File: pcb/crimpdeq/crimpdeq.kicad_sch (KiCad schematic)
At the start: 53 parts, among them J2 USB4105-GF-A, Q1 S8550, Q2 DMG3415U, SW1 SW_Push, SW2 SW_Push, U1 ESP32-C3-MINI-1, U2 MCP73831T-2ACI/OT, U3 HX711, U4 Rust_Board, U6 SY8088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

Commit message: fix: add assembly notes for manufacturing
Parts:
- J2: AssemblyNote (none) -> Approved alternate: TYPE-C-31-M-12 may be assembled if foot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
- Q1: AssemblyNote (none) -> TH part: assemble TO-92 inline S8550 only. Do not substitut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
- R12: AssemblyNote (none) -> Critical value: 33kΩ 0402 resistor. Do not use 10kΩ.
- R5: AssemblyNote (none) -> Critical value: 12kΩ 0402 resistor. Do not use 100kΩ.
- R6: AssemblyNote (none) -> Critical value: 8.2kΩ 0402 resistor. Do not use 100kΩ.
- R7, R8: AssemblyNote (none) -> Critical value: 100Ω 0402 resistor. Do not use 100kΩ.
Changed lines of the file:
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@@
 			)
 		)
+		(property "AssemblyNote" "Critical value: 33kΩ 0402 resistor. Do not use 10kΩ."
+			(at 172.72 71.12 0)
+			(effects
+				(font
+					(size 1.27 1.27)
+				)
+				(hide yes)
+			)
+		)
 		(pin "1"
 		)
@@
 			)
 		)
+		(property "AssemblyNote" "Critical value: 12kΩ 0402 resistor. Do not use 100kΩ."
+			(at 72.39 137.16 0)
+			(effects
+				(font
+					(size 1.27 1.27)
+				)
+				(hide yes)
+			)
+		)
 		(pin "1"
 		)
@@
 			)
 		)
+		(property "AssemblyNote" "TH part: assemble TO-92 inline S8550 only. Do not substitute an SMD package."
+			(at 74.93 125.73 0)
+			(effects
+				(font
+					(size 1.27 1.27)
+				)
+				(hide yes)
+			)
+		)
 		(pin "1"
 		)
@@
 			)
 		)
+		(property "AssemblyNote" "Approved alternate: TYPE-C-31-M-12 may be assembled if footprint, pinout, and shell tabs match USB4105-GF-A."
+			(at 213.36 39.37 0)
+			(effects
+				(font
+					(size 1.27 1.27)
+				)
+				(hide yes)
+			)
+		)
 		(pin "A1_B12"
 		)
@@
 			)
 		)
+		(property "AssemblyNote" "Critical value: 8.2kΩ 0402 resistor. Do not use 100kΩ."
+			(at 67.31 140.97 0)
+			(effects
+				(font
+					(size 1.27 1.27)
+				)
+				(hide yes)
+			)
+		)
 		(pin "1"
 		)
@@
 			)
 		)
+		(property "AssemblyNote" "Critical value: 100Ω 0402 resistor. Do not use 100kΩ."
+			(at 31.75 146.05 0)
+			(effects
+				(font
+					(size 1.27 1.27)
+				)
+				(hide yes)
+			)
+		)
 		(pin "1"
 		)
@@
 			(at 31.75 153.67 0)
 			(effects
+				(font
+					(size 1.27 1.27)
+				)
+				(hide yes)
+			)
+		)
+		(property "AssemblyNote" "Critical value: 100Ω 0402 resistor. Do not use 100kΩ."
+			(at 31.75 153.67 0)
+			(effects

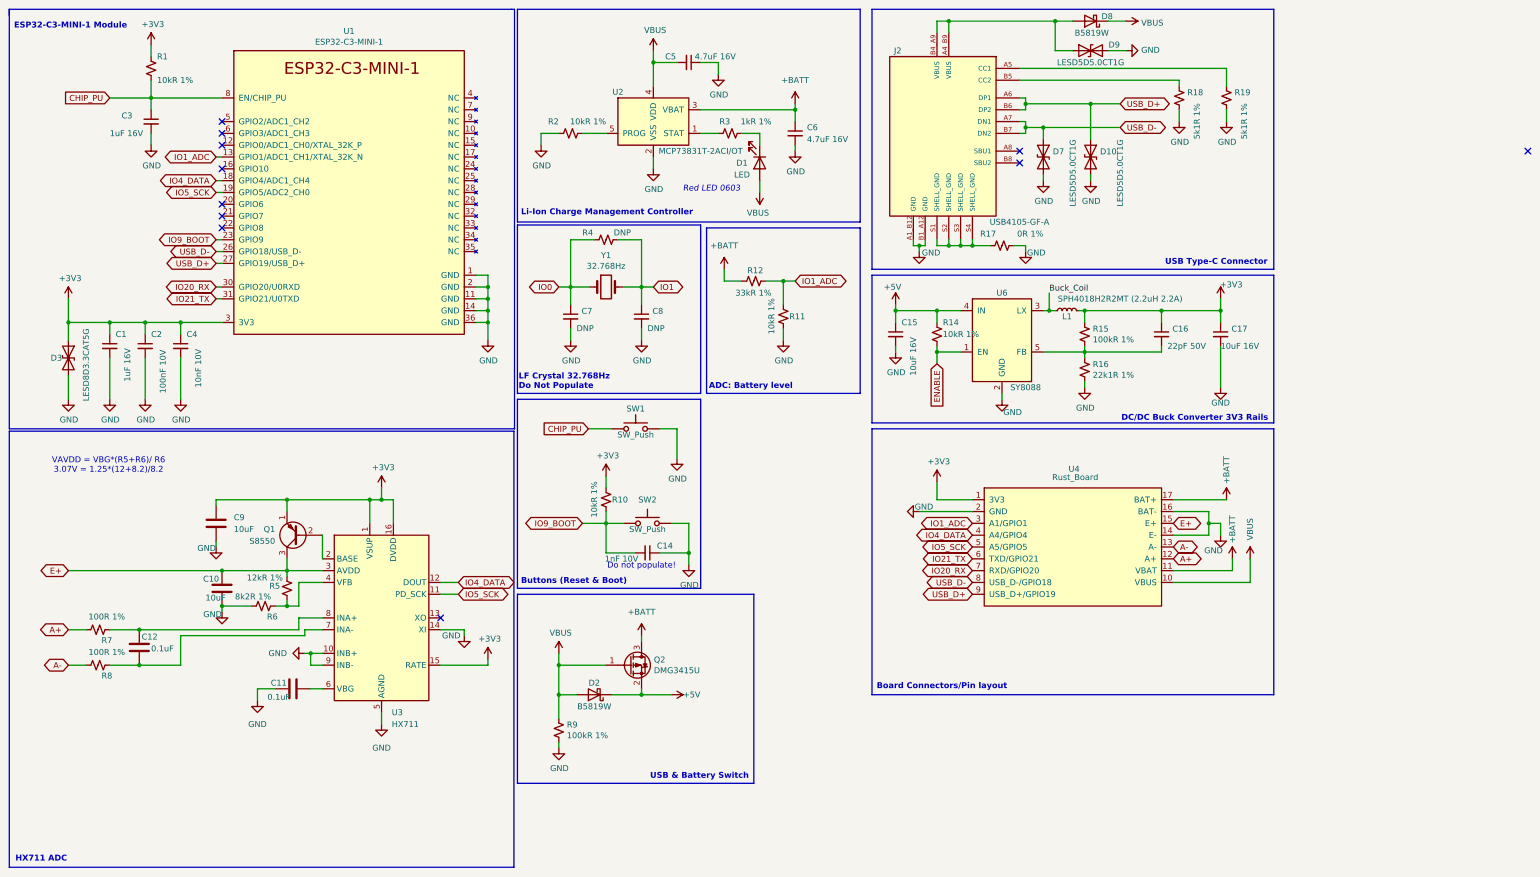
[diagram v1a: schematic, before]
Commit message: fix: resolve KiCad ERC and DRC failures
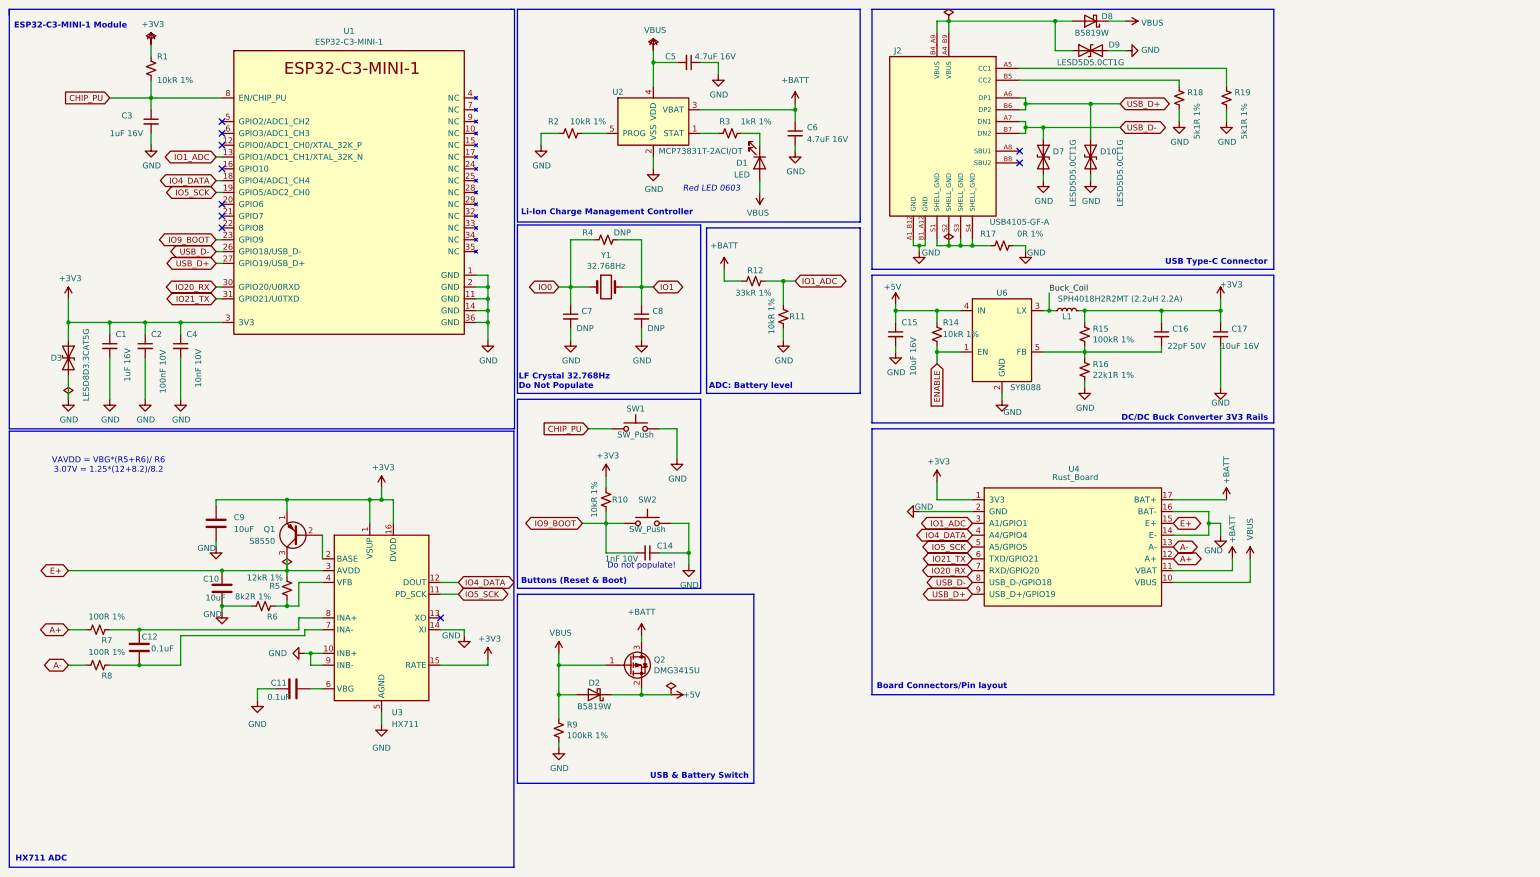
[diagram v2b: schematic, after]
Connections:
- no-connect marks 11 -> 10

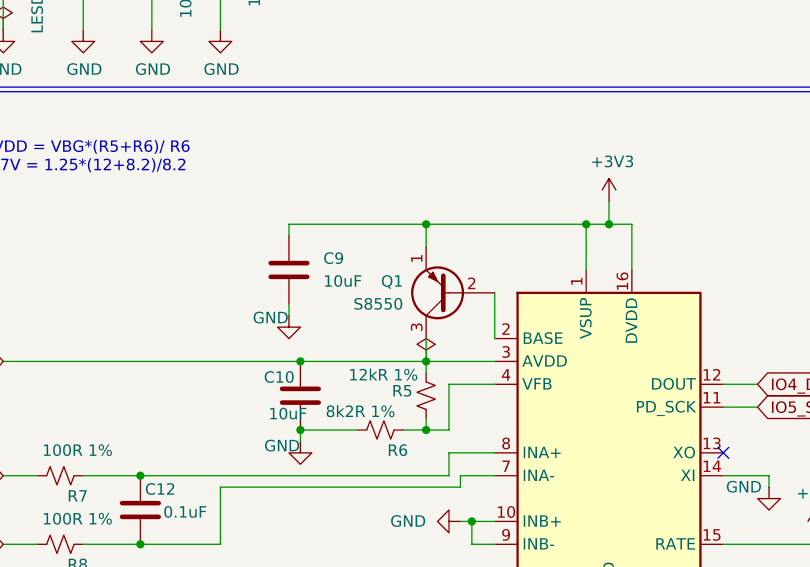
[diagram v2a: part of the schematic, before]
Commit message: fix: switch Q1 to SOT-23 SS8550
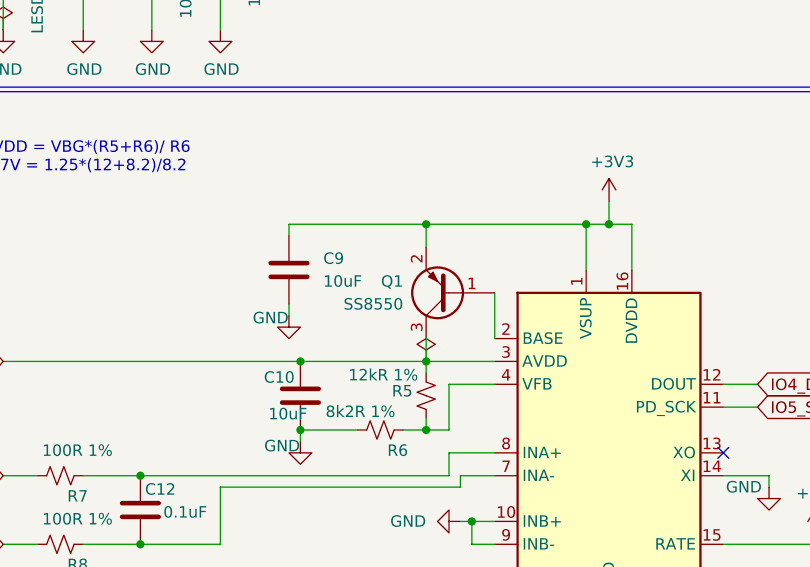
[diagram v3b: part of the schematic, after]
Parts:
- Q1: value S8550 -> SS8550; footprint Package_TO_SOT_THT:TO-92_Inline -> Package_TO_SOT_SMD:SOT-23; symbol Transistor_BJT:S8550 -> Transistor_BJT:SS8550; AssemblyNote TH part: assemble TO-92 inline S8550 only. Do not substitut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 -> (none)
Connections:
- net +3V3: now also Q1.2 (E); no longer Q1.1 (E)
- net at U3.2 (BASE): now also Q1.1 (B); no longer Q1.2 (B)
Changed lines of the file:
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@@
 	)
 	(symbol
-		(lib_id "Transistor_BJT:S8550")
+		(lib_id "Transistor_BJT:SS8550")
 		(at 74.93 125.73 180)
 		(unit 1)
@@
 			)
 		)
-		(property "Value" "S8550"
+		(property "Value" "SS8550"
 			(at 69.85 126.9999 0)
 			(effects
@@
 			)
 		)
-		(property "Footprint" "Package_TO_SOT_THT:TO-92_Inline"
+		(property "Footprint" "Package_TO_SOT_SMD:SOT-23"
 			(at 69.85 123.825 0)
 			(effects
@@
 			)
 		)
-		(property "Datasheet" "http://www.unisonic.com.tw/datasheet/S8550.pdf"
+		(property "Datasheet" "http://www.secosgmbh.com/datasheet/products/SSMPTransistor/SOT-23/SS8550.pdf"
 			(at 74.93 125.73 0)
 			(effects
@@
 			)
 		)
-		(property "Description" "0.7A Ic, 20V Vce, Low Voltage High Current PNP Transistor, TO-92"
+		(property "Description" "General Purpose PNP Transistor, 1.5A Ic, 25V Vce, SOT-23"
 			(at 74.93 125.73 0)
 			(effects
@@
 			)
 		)
-		(property "AssemblyNote" "TH part: assemble TO-92 inline S8550 only. Do not substitute an SMD package."
+		(property "AssemblyNote" ""
 			(at 74.93 125.73 0)
 			(effects

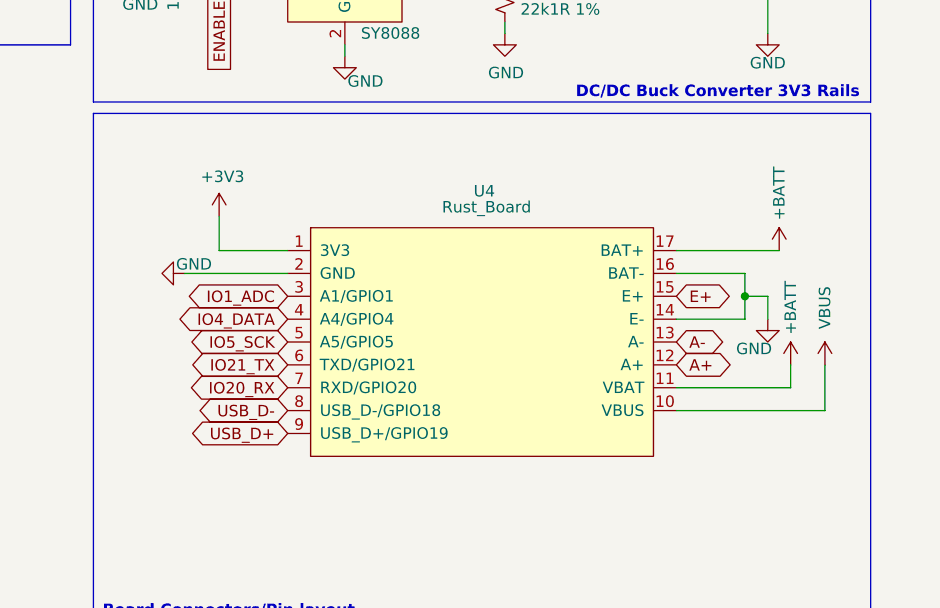
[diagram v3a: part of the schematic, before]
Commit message: fix: trim U4 pads and reroute board
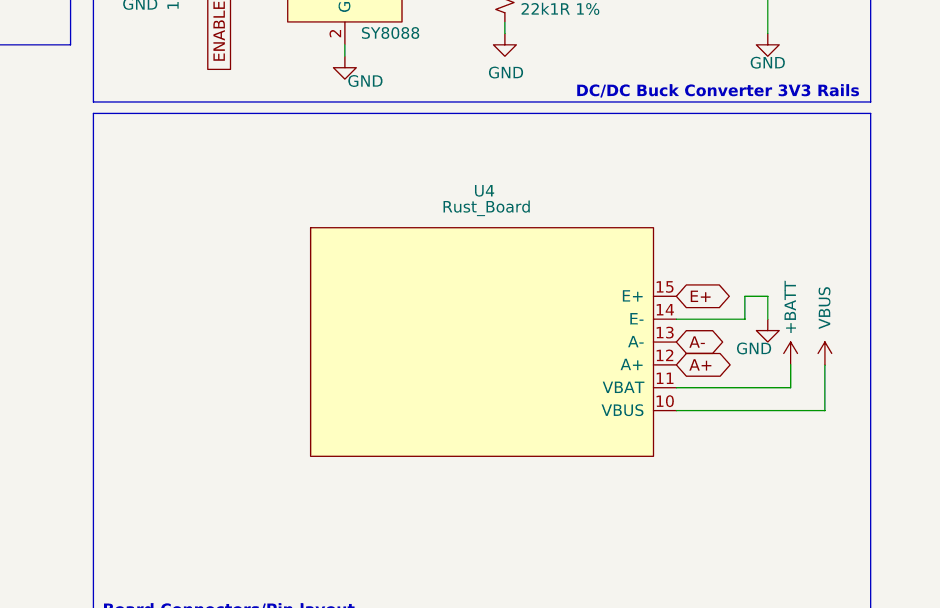
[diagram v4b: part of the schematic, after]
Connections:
- net +3V3: no longer U4.1 (3V3)
- net +BATT: no longer U4.17 (BAT+)
- net GND: no longer U4.16 (BAT-), U4.2 (GND)
- net IO1_ADC: no longer U4.3 (A1/GPIO1)
- net IO20_RX: no longer U4.7 (RXD/GPIO20)
- net IO21_TX: no longer U4.6 (TXD/GPIO21)
- net IO4_DATA: no longer U4.4 (A4/GPIO4)
- net IO5_SCK: no longer U4.5 (A5/GPIO5)
- net USB_D+: no longer U4.9 (USB_D+/GPIO19)
- net USB_D-: no longer U4.8 (USB_D-/GPIO18)

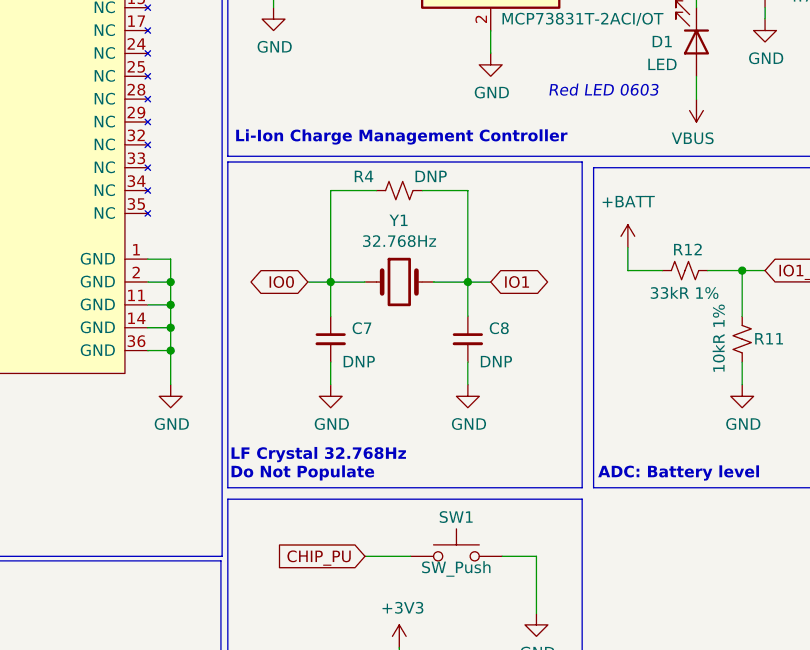
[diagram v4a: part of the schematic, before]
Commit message: fix: remove unused rtc crystal option
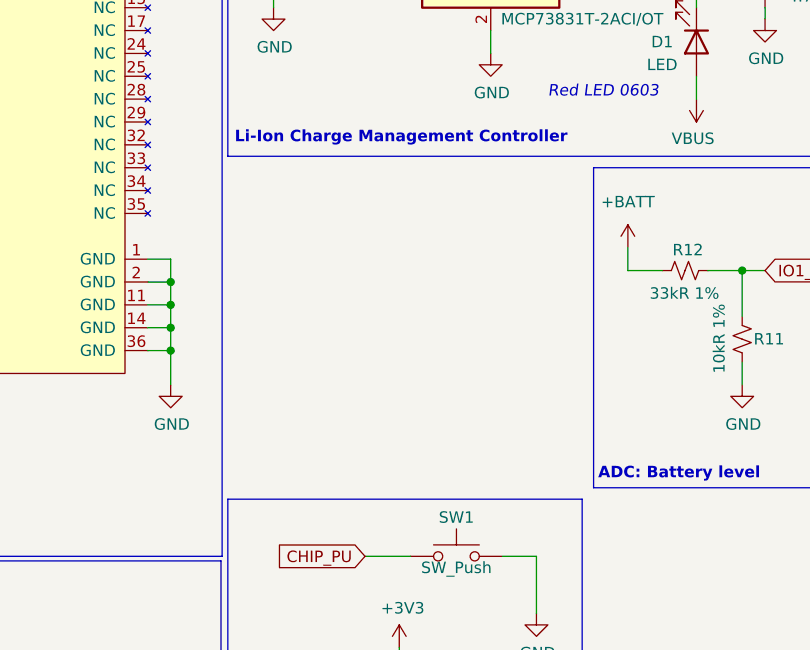
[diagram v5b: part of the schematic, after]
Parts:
- removed C7, C8: DNP, Capacitor_SMD:C_0402_1005Metric, symbol Device:C_Small
- removed R4: DNP, Resistor_SMD:R_0402_1005Metric, symbol Device:R_Small_US
- removed Y1: 32.768Hz, Crystal:Crystal_SMD_3215-2Pin_3.2x1.5mm, symbol Device:Crystal
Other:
- note removed: "LF Crystal 32.768Hz Do Not Populate"
